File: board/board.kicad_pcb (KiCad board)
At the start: 2 copper layers, 21 x 29 mm, 5 parts, among them J1 019_100BASE-T_with_CT, J2 009_1000BASE-T, J3 004_BASE-T_CT

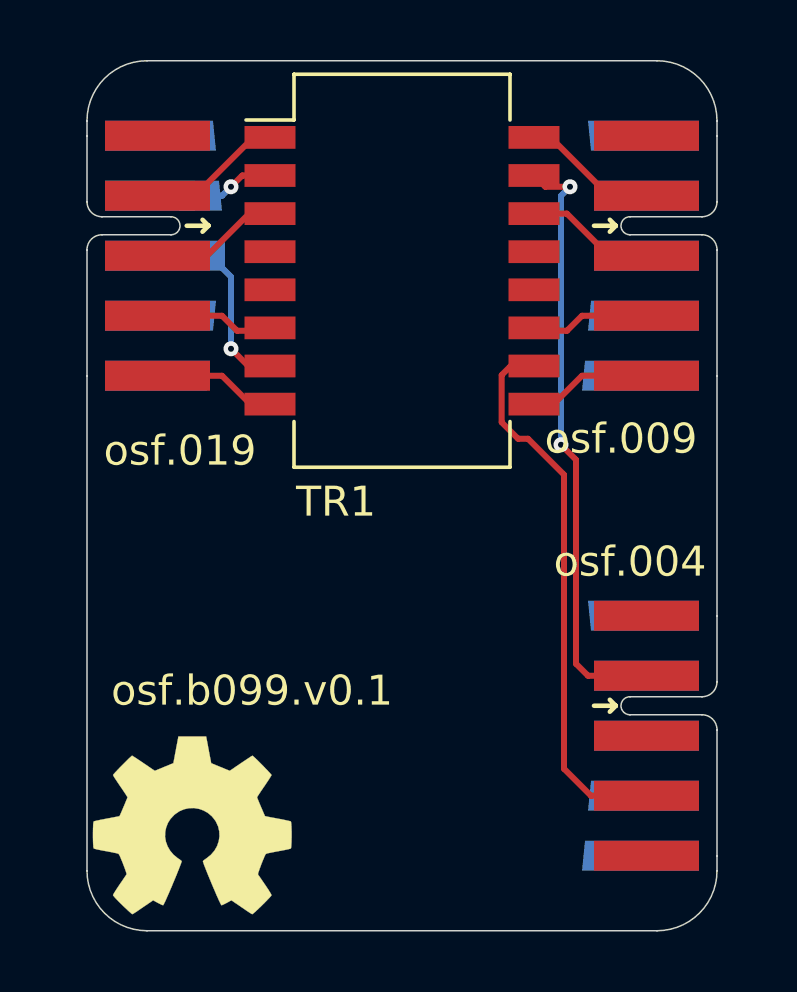
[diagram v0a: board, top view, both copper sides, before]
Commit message: updated to use put_on_edge v1.0 connectors
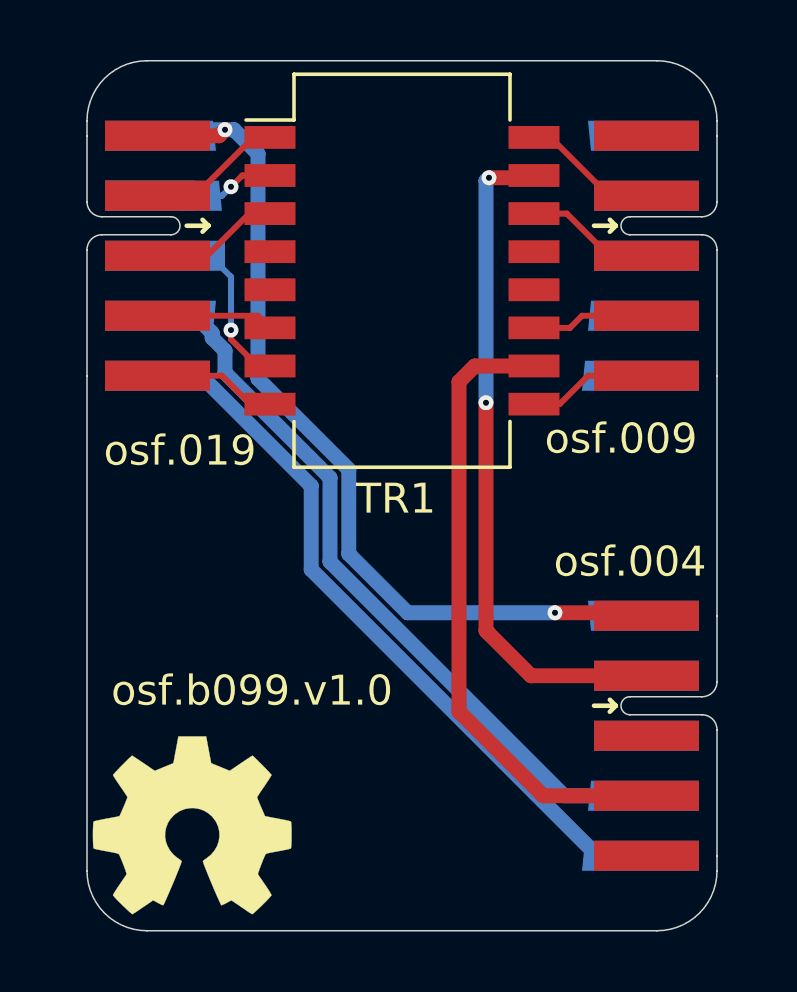
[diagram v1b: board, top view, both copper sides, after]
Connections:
- J1 pad 1: unconnected-(J1-Pad1) -> GND
- J1 pad 10: (no net) -> Net-(J1-Pad10)
- J1 pad 6: unconnected-(J1-Pad6) -> GND
- J1 pad 9: (no net) -> Net-(J1-Pad9)
- J3 pad 1: unconnected-(J3-Pad1) -> GND
- J3 pad 10: unconnected-(J3-Pad10) -> Net-(J1-Pad10)
- J3 pad 3: unconnected-(J3-Pad3) -> (no net)
- J3 pad 5: unconnected-(J3-Pad5) -> (no net)
- J3 pad 7: unconnected-(J3-Pad7) -> (no net)
- J3 pad 9: unconnected-(J3-Pad9) -> Net-(J1-Pad9)
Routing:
- net GND: track 0.00 -> 31.4 mm, vias 0 -> 2
- net Net-(J1-Pad9): track 0.00 -> 25.0 mm
- net Net-(J1-Pad10): track 0.00 -> 24.5 mm
- net /eth_magnetics/CT2: track 18.5 -> 21.1 mm
- net /eth_magnetics/CT1: track 20.1 -> 22.6 mm
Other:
- board text added: "osf.b099.v1.0"
- board text removed: "osf.b099.v0.1"
